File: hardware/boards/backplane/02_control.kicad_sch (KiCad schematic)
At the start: 14 parts, among them J10 SWD, U1 STM32C092GCU6

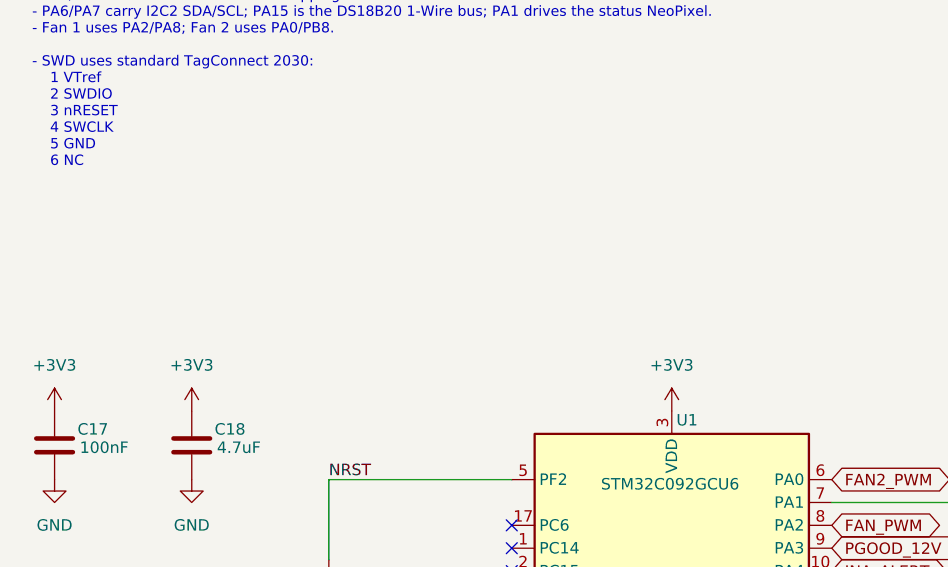
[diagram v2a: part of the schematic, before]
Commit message: Refine prototype Kelvin pours and input grounding; add test TODOs
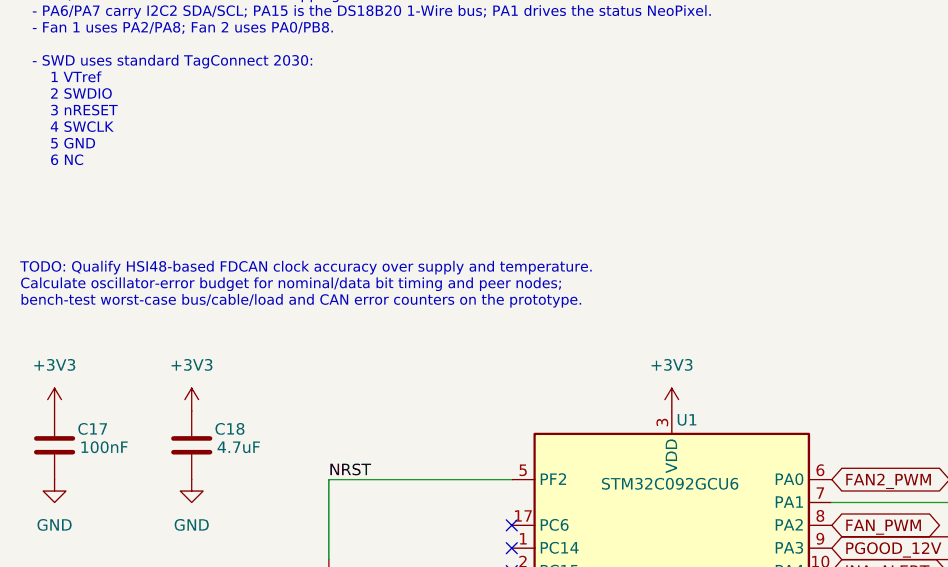
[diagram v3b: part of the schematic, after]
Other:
- note added: "TODO: Qualify HSI48-based FDCAN clock accuracy over supply and temperature. Calculate oscillator-error budget for nominal/data bit timing and peer nodes; bench-test worst-case bus/cable/load and CAN error counters on the prototype."
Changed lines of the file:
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@@
 	(generator_version "10.0")
 	(paper "A4")
+	(text "TODO: Qualify HSI48-based FDCAN clock accuracy over supply and temperature.\nCalculate oscillator-error budget for nominal/data bit timing and peer nodes;\nbench-test worst-case bus/cable/load and CAN error counters on the prototype."
+		(exclude_from_sim no)
+		(at 16.51 62.23 0)
+		(effects
+			(font
+				(size 1.143 1.143)
+			)
+			(justify left bottom)
+		)
+	)
 	(text "STM32C092GCU6 / Housekeeping"
 		(exclude_from_sim no)
